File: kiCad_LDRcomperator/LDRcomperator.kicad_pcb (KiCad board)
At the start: 2 copper layers, 47.5 x 45 mm, 14 parts, among them J1 Screw_Terminal_01x02, J2 Conn_01x02_MountingPin, J3 Conn_01x02_MountingPin

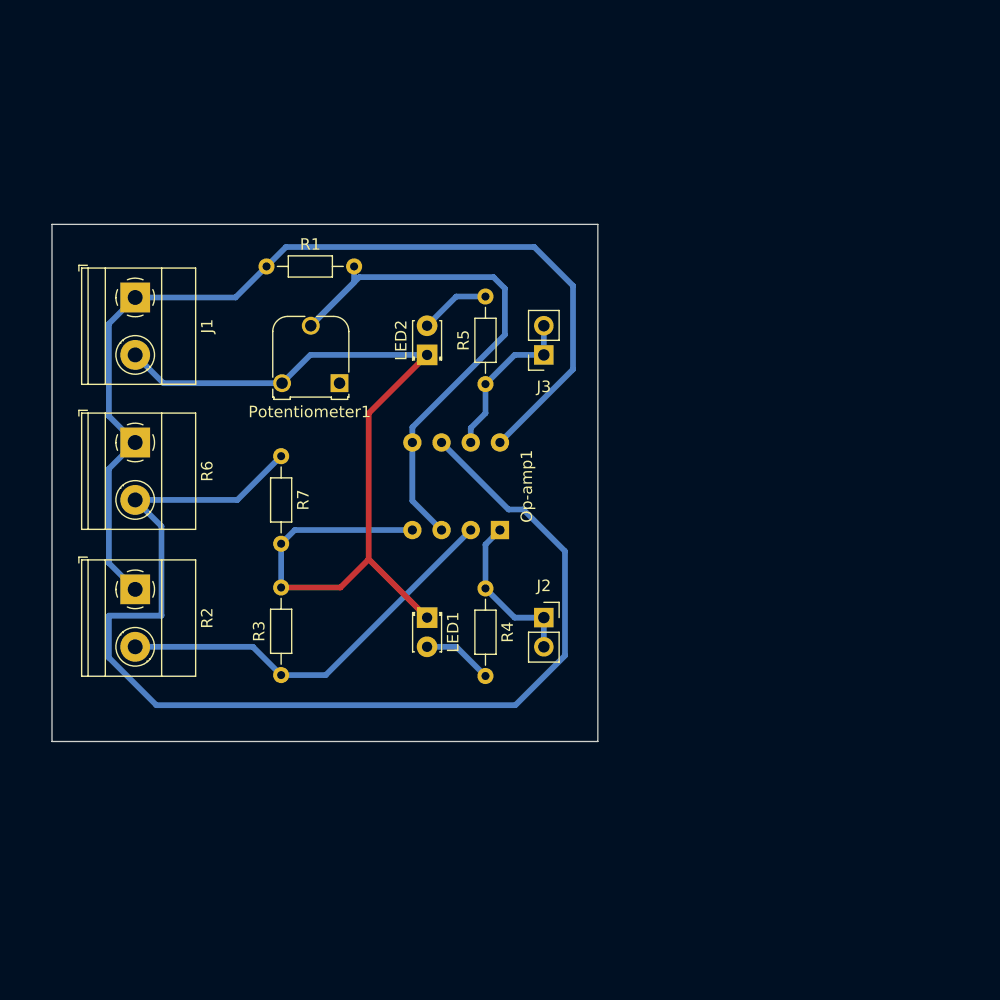
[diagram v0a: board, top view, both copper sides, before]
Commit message: kicad improvments for ldrCompartor
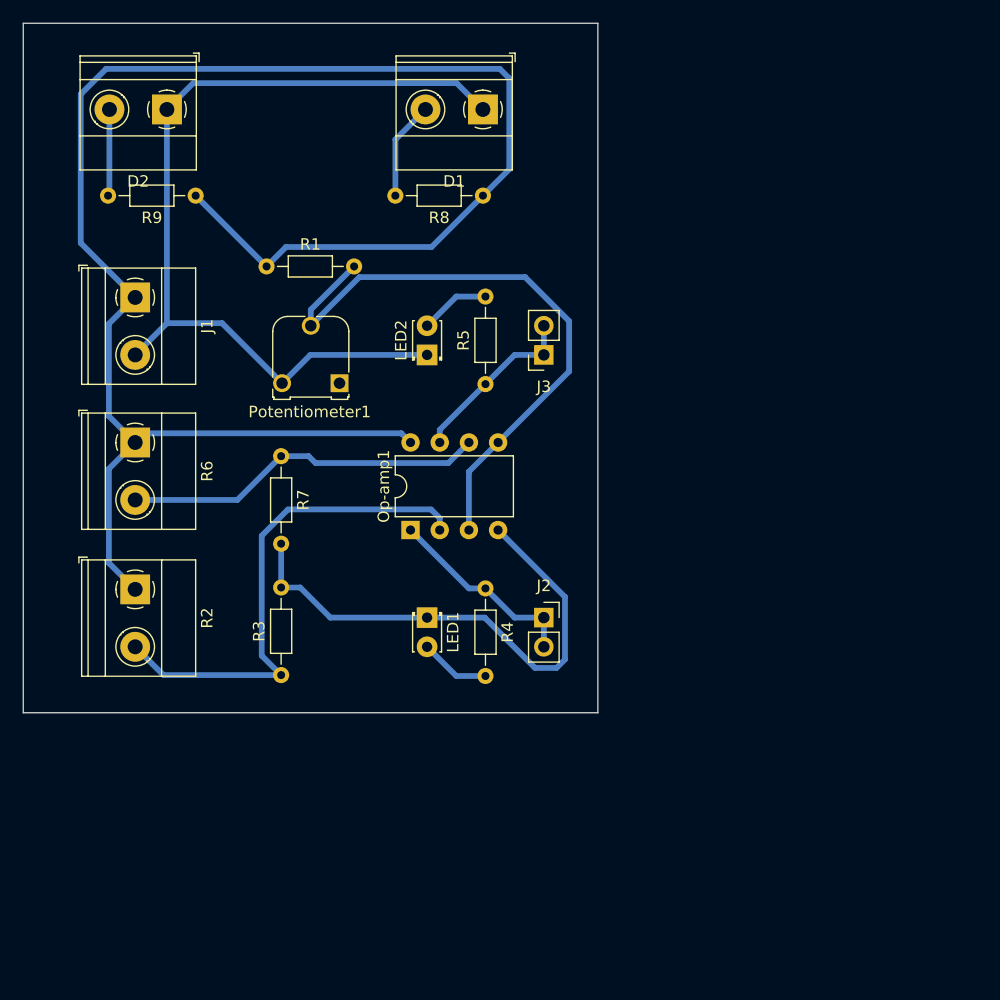
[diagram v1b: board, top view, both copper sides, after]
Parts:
- added D1: LED, TerminalBlock_Phoenix:TerminalBlock_Phoenix_MKDS-1,5-2_1x02_P5.00mm_Horizontal, F.Cu at (172.5, 65.0)
- added D2: LED, TerminalBlock_Phoenix:TerminalBlock_Phoenix_MKDS-1,5-2_1x02_P5.00mm_Horizontal, F.Cu at (145.0, 65.0)
- added R8: 30, Resistor_THT:R_Axial_DIN0204_L3.6mm_D1.6mm_P7.62mm_Horizontal, F.Cu at (172.5, 72.5)
- added R9: 30, Resistor_THT:R_Axial_DIN0204_L3.6mm_D1.6mm_P7.62mm_Horizontal, F.Cu at (147.5, 72.5)
- Op-amp1: moved to F.Cu
- Potentiometer1: value 10k ohm -> 100k ohm
- R1: value 2.2k -> 22k ohm
- moved Op-amp1 7.78 mm to (166.2, 101.6)
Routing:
- net Net-(Op-amp1---Pad6): track 100.5 -> 31.6 mm
- net +3V3: track 86.8 -> 153.3 mm
- net GND: track 78.9 -> 123.1 mm
- net Net-(Op-amp1---Pad2): track 35.4 -> 44.3 mm
- net Net-(D1-A): track 0.00 -> 8.59 mm
- net Net-(D2-A): track 0.00 -> 7.55 mm
- net Net-(Op-amp1-+-Pad3): track 51.2 -> 54.3 mm
- net Net-(J2-Pin_1): track 14.3 -> 17.3 mm
- net Net-(J3-Pin_1): track 14.3 -> 15.4 mm
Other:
- board size 47.5 x 45 mm -> 50 x 60 mm

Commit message: KiCad changes
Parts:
- R3: value 2,2k ohm -> 2k ohm
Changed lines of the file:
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@@
 			)
 		)
-		(property "Value" "2,2k ohm"
+		(property "Value" "2k ohm"
 			(at 3.81 1.92 90)
 			(layer "F.Fab")

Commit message: Rapporten
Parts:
- D1, D2, J1, J2, J3, LED1, LED2, Op-amp1, Potentiometer1, R1, R2, R3, R4, R5, R6, R7, R8, R9: moved to B.Cu
- moved D2 89.1 mm to (207.9, 128.0), turned to -90 degrees
- moved R9 74.9 mm to (200.4, 125.5), turned to -90 degrees
- moved J1 69.8 mm to (191.6, 130.8), turned to 180 degrees
- moved R1 57.5 mm to (194.3, 119.3), turned to 90 degrees
- moved R6 52.0 mm to (179.0, 130.8), turned to 180 degrees
- moved D1 50.2 mm to (207.9, 100.5), turned to -90 degrees
- moved R8 39.6 mm to (200.4, 100.5), turned to -90 degrees
- moved Potentiometer1 34.1 mm to (184.1, 113.0), turned to -90 degrees
- moved R2 33.9 mm to (166.2, 130.8), turned to 180 degrees
- moved R7 32.3 mm to (177.8, 118.1), turned to 180 degrees
- moved LED2 26.8 mm to (186.6, 105.4), turned to 0 degrees
- moved J2 19.9 mm to (163.7, 95.2), turned to 90 degrees
- moved R5 16.1 mm to (184.0, 100.3), turned to 0 degrees
- moved J3 12.5 mm to (186.6, 95.2), turned to -90 degrees
- moved R4 9.09 mm to (166.3, 100.3), turned to 180 degrees
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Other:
- board size 50 x 60 mm -> 60 x 50 mm
